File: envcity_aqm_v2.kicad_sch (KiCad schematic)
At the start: 136 parts, among them IC1 DS1307ZN+, IC2 DMMT5401-7F, IC3 DMMT5401-7F, IC4 DMMT5401-7-F, IC6 ESP32-S2-SOLO-N4R2, J1 USB_B_Micro, J10 Conn_01x06_Male, J11 Conn_01x06_Male, J12 Conn_01x06_Male, J13 Conn_01x06_Male, J14 Conn_01x08_Pin, J15 Conn_01x02_Male, J16 Conn_01x02_Male, J2 Screw_Terminal_01x02, J3 Screw_Terminal_01x02, J4 Micro_SD_Card, J5 Conn_01x03_Male, J6 Conn_01x04_Male, J7 Conn_01x06_Pin, J8 Conn_01x06_Male, J9 Conn_01x06_Male, Q1 DMG2301L / DMP2045U, Q2 DMG2301L / DMP2045U, Q3 DMG2301L, Q4 DMG2301L, Q5 DMG2301L / DMP2045U, Q6 DMG2301L, Q7 DMN10H220L, Q8 DMN10H220L, SW1 BOOT, SW1 RESET, U1 TP4056, U10 RFM95W-915S2, U11 ADS1115IDGS, U2 USBLC6-2SC6, U3 MT3608, U4 MT3608, U5 LM2596S-5, U6 AP2112K-3.3, U7 DHT11, U8 AP2112K-3.3, U9 74HC4067DB, Y2 AB26TRB

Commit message: Terminando o posicionamento dos components
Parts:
- added C35: 100nF, Capacitor_SMD:C_0603_1608Metric, symbol Device:C_Small
- C18, C19, C20, C21, C25, C26, C27: footprint Capacitor_SMD:C_0805_2012Metric -> Capacitor_SMD:C_0603_1608Metric
- J14: footprint Connector_PinHeader_2.54mm:PinHeader_1x08_P2.54mm_Vertical -> Connector_Molex:Molex_PicoBlade_53047-0810_1x08_P1.25mm_Vertical
- J7: footprint Connector_Molex:Molex_KK-254_AE-6410-06A_1x06_P2.54mm_Vertical -> Connector_PinHeader_2.54mm:PinHeader_1x06_P2.54mm_Vertical
- renumbered J8 to EQ1, J9 to EQ2, J10 to EQ3, J11 to EQ4
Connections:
- net +5V: now also C35.2
- net GND: now also C35.1
- net I12: now also J5.3 (Pin_3)
- net I7: no longer J5.3 (Pin_3)
- net RFM_CS: now also IC6.17 (IO9); no longer IC6.18 (IO10)
- net RFM_DIO0: now also IC6.25 (IO34); no longer IC6.23 (IO21)
- net RFM_DIO2: now also IC6.23 (IO21); no longer IC6.25 (IO34)
- net RFM_SCK: now also IC6.18 (IO10); no longer IC6.21 (IO13)
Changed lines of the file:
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@@
   (junction (at 213.36 238.76) (diameter 0) (color 0 0 0 0)
   )
+  (junction (at 90.17 285.75) (diameter 0) (color 0 0 0 0)
+  )
   (junction (at 361.95 261.62) (diameter 0) (color 0 0 0 0)
   )
@@
   (no_connect (at 66.04 337.82))
   (no_connect (at 486.41 270.51))
+  (no_connect (at 462.28 203.2))
   (no_connect (at 486.41 275.59))
   (no_connect (at 495.3 157.48))
@@
   (no_connect (at 334.01 196.85))
   (no_connect (at 462.28 180.34))
-  (no_connect (at 462.28 193.04))
   (no_connect (at 468.63 78.74))
   (no_connect (at 495.3 162.56))
@@
     (stroke (width 0) (type default))
   )
+  (wire (pts (xy 90.17 285.75) (xy 96.52 285.75))
+    (stroke (width 0) (type default))
+  )
   (wire (pts (xy 152.4 317.5) (xy 152.4 322.58))
     (stroke (width 0) (type default))
@@
     (stroke (width 0) (type default))
   )
-  (wire (pts (xy 457.2 195.58) (xy 462.28 195.58))
+  (wire (pts (xy 457.2 193.04) (xy 462.28 193.04))
     (stroke (width 0) (type default))
   )
@@
     (stroke (width 0) (type default))
   )
-  (wire (pts (xy 457.2 203.2) (xy 462.28 203.2))
+  (wire (pts (xy 457.2 195.58) (xy 462.28 195.58))
     (stroke (width 0) (type default))
   )
@@
     (stroke (width 0) (type default))
   )
+  (wire (pts (xy 101.6 285.75) (xy 102.87 285.75))
+    (stroke (width 0) (type default))
+  )
   (wire (pts (xy 501.65 195.58) (xy 501.65 198.12))
     (stroke (width 0) (type default))
@@
     (effects (font (size 1.27 1.27)) (justify left bottom))
   )
-  (label "RFM_DIO0" (at 457.2 208.28 180) (fields_autoplaced)
+  (label "RFM_DIO0" (at 457.2 213.36 180) (fields_autoplaced)
     (effects (font (size 1.27 1.27)) (justify right bottom))
   )
@@
     (effects (font (size 1.27 1.27)) (justify left bottom))
   )
-  (label "RFM_SCK" (at 457.2 203.2 180) (fields_autoplaced)
+  (label "RFM_SCK" (at 457.2 195.58 180) (fields_autoplaced)
     (effects (font (size 1.27 1.27)) (justify right bottom))
   )
@@
     (effects (font (size 1.27 1.27)) (justify left bottom))
   )
-  (label "RFM_DIO2" (at 457.2 213.36 180) (fields_autoplaced)
+  (label "RFM_DIO2" (at 457.2 208.28 180) (fields_autoplaced)
     (effects (font (size 1.27 1.27)) (justify right bottom))
   )
@@
     (effects (font (size 1.27 1.27)) (justify left bottom))
   )
-  (label "I7" (at 294.64 234.95 0) (fields_autoplaced)
+  (label "I12" (at 294.64 234.95 0) (fields_autoplaced)
     (effects (font (size 1.27 1.27)) (justify left bottom))
   )
@@
     (effects (font (size 1.27 1.27)) (justify right bottom))
   )
-  (label "RFM_CS" (at 457.2 195.58 180) (fields_autoplaced)
+  (label "RFM_CS" (at 457.2 193.04 180) (fields_autoplaced)
     (effects (font (size 1.27 1.27)) (justify right bottom))
   )
@@
   (symbol (lib_id "envcity_aqm_v2-rescue:Conn_01x06_Male-Connector") (at 325.12 227.33 0) (unit 1)
     (in_bom yes) (on_board yes) (dnp no)
-    (property "Reference" "J8" (at 327.66 215.9 0)
+    (property "Reference" "EQ1" (at 327.66 215.9 0)
       (effects (font (size 1.27 1.27)))
     )
@@
       (project "envcity_aqm_v2"
         (path "/332e6a95-8453-45a7-bff6-50b465637d27"
-          (reference "J8") (unit 1)
+          (reference "EQ1") (unit 1)
         )
       )
@@
   (symbol (lib_id "envcity_aqm_v2-rescue:Conn_01x06_Male-Connector") (at 350.52 227.33 0) (unit 1)
     (in_bom yes) (on_board yes) (dnp no)
-    (property "Reference" "J9" (at 353.06 215.9 0)
+    (property "Reference" "EQ2" (at 353.06 215.9 0)
       (effects (font (size 1.27 1.27)))
     )
@@
       (project "envcity_aqm_v2"
         (path "/332e6a95-8453-45a7-bff6-50b465637d27"
-          (reference "J9") (unit 1)
+          (reference "EQ2") (unit 1)
         )
       )
@@
   (symbol (lib_id "envcity_aqm_v2-rescue:Conn_01x06_Male-Connector") (at 325.12 252.73 0) (unit 1)
     (in_bom yes) (on_board yes) (dnp no)
-    (property "Reference" "J10" (at 327.66 241.3 0)
+    (property "Reference" "EQ3" (at 327.66 241.3 0)
       (effects (font (size 1.27 1.27)))
     )
@@
       (project "envcity_aqm_v2"
         (path "/332e6a95-8453-45a7-bff6-50b465637d27"
-          (reference "J10") (unit 1)
+          (reference "EQ3") (unit 1)
         )
       )
@@
   (symbol (lib_id "envcity_aqm_v2-rescue:Conn_01x06_Male-Connector") (at 350.52 254 0) (unit 1)
     (in_bom yes) (on_board yes) (dnp no)
-    (property "Reference" "J11" (at 353.06 241.3 0)
+    (property "Reference" "EQ4" (at 353.06 241.3 0)
       (effects (font (size 1.27 1.27)))
     )
@@
       (project "envcity_aqm_v2"
         (path "/332e6a95-8453-45a7-bff6-50b465637d27"
-          (reference "J11") (unit 1)
+          (reference "EQ4") (unit 1)
         )
       )
@@
       (effects (font (size 1.27 1.27)) (justify left))
     )
-    (property "Footprint" "Capacitor_SMD:C_0805_2012Metric" (at 367.03 227.33 0)
+    (property "Footprint" "Capacitor_SMD:C_0603_1608Metric" (at 367.03 227.33 0)
       (effects (font (size 1.27 1.27)) hide)
     )
@@
       (effects (font (size 1.27 1.27)) (justify left))
     )
-    (property "Footprint" "Capacitor_SMD:C_0805_2012Metric" (at 341.63 227.33 0)
+    (property "Footprint" "Capacitor_SMD:C_0603_1608Metric" (at 341.63 227.33 0)
       (effects (font (size 1.27 1.27)) hide)
     )
@@
       (effects (font (size 1.27 1.27)) (justify left))
     )
-    (property "Footprint" "Capacitor_SMD:C_0805_2012Metric" (at 340.36 252.73 0)
+    (property "Footprint" "Capacitor_SMD:C_0603_1608Metric" (at 340.36 252.73 0)
       (effects (font (size 1.27 1.27)) hide)
     )
@@
       (effects (font (size 1.27 1.27)) (justify left))
     )
-    (property "Footprint" "Capacitor_SMD:C_0805_2012Metric" (at 365.76 252.73 0)
+    (property "Footprint" "Capacitor_SMD:C_0603_1608Metric" (at 365.76 252.73 0)
       (effects (font (size 1.27 1.27)) hide)
     )
@@
     )
   )
+  (symbol (lib_id "Device:C_Small") (at 99.06 285.75 270) (mirror x) (unit 1)
+    (in_bom yes) (on_board yes) (dnp no)
+    (property "Reference" "C35" (at 100.2284 283.4132 0)
+      (effects (font (size 1.27 1.27)) (justify left))
+    )
+    (property "Value" "100nF" (at 97.917 283.4132 0)
+      (effects (font (size 1.27 1.27)) (justify left))
+    )
+    (property "Footprint" "Capacitor_SMD:C_0603_1608Metric" (at 99.06 285.75 0)
+      (effects (font (size 1.27 1.27)) hide)
+    )
+    (property "Datasheet" "~" (at 99.06 285.75 0)
+      (effects (font (size 1.27 1.27)) hide)
+    )
+    (pin "1")
+    (pin "2")
+    (instances
+      (project "envcity_aqm_v2"
+        (path "/332e6a95-8453-45a7-bff6-50b465637d27"
+          (reference "C35") (unit 1)
+        )
+      )
+    )
+  )
   (symbol (lib_id "DMMT5401-7-F:DMMT5401-7-F") (at 247.65 34.29 0) (mirror x) (unit 2)
     (in_bom yes) (on_board yes) (dnp no)
@@
       (effects (font (size 1.27 1.27)) (justify left))
     )
-    (property "Footprint" "Capacitor_SMD:C_0805_2012Metric" (at 365.76 278.13 0)
+    (property "Footprint" "Capacitor_SMD:C_0603_1608Metric" (at 365.76 278.13 0)
       (effects (font (size 1.27 1.27)) hide)
     )
@@
       (effects (font (size 1.27 1.27)))
     )
-    (property "Footprint" "Connector_Molex:Molex_KK-254_AE-6410-06A_1x06_P2.54mm_Vertical" (at 285.75 313.69 0)
+    (property "Footprint" "Connector_PinHeader_2.54mm:PinHeader_1x06_P2.54mm_Vertical" (at 285.75 313.69 0)
       (effects (font (size 1.27 1.27)) hide)
     )
@@
       (effects (font (size 1.27 1.27)) (justify left))
     )
-    (property "Footprint" "Capacitor_SMD:C_0805_2012Metric" (at 340.36 278.13 0)
+    (property "Footprint" "Capacitor_SMD:C_0603_1608Metric" (at 340.36 278.13 0)
       (effects (font (size 1.27 1.27)) hide)
     )
@@
       (effects (font (size 1.27 1.27)))
     )
-    (property "Footprint" "Connector_PinHeader_2.54mm:PinHeader_1x08_P2.54mm_Vertical" (at 328.93 186.69 0)
+    (property "Footprint" "Connector_Molex:Molex_PicoBlade_53047-0810_1x08_P1.25mm_Vertical" (at 328.93 186.69 0)
       (effects (font (size 1.27 1.27)) hide)
     )
@@
     )
   )
+  (symbol (lib_id "power:GND") (at 102.87 285.75 90) (unit 1)
+    (in_bom yes) (on_board yes) (dnp no) (fields_autoplaced)
+    (property "Reference" "#PWR0108" (at 109.22 285.75 0)
+      (effects (font (size 1.27 1.27)) hide)
+    )
+    (property "Value" "GND" (at 106.045 286.0668 90)
+      (effects (font (size 1.27 1.27)) (justify right))
+    )
+    (property "Footprint" "" (at 102.87 285.75 0)
+      (effects (font (size 1.27 1.27)) hide)
+    )
+    (property "Datasheet" "" (at 102.87 285.75 0)
+      (effects (font (size 1.27 1.27)) hide)
+    )
+    (pin "1")
+    (instances
+      (project "envcity_aqm_v2"
+        (path "/332e6a95-8453-45a7-bff6-50b465637d27"
+          (reference "#PWR0108") (unit 1)
+        )
+      )
+    )
+  )
   (symbol (lib_id "power:+3V3") (at 354.33 177.8 0) (unit 1)
     (in_bom yes) (on_board yes) (dnp no) (fields_autoplaced)
@@
       (effects (font (size 1.27 1.27)) (justify left))
     )
-    (property "Footprint" "Capacitor_SMD:C_0805_2012Metric" (at 342.9 179.07 0)
+    (property "Footprint" "Capacitor_SMD:C_0603_1608Metric" (at 342.9 179.07 0)
       (effects (font (size 1.27 1.27)) hide)
     )

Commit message: mudando posicoes
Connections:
- net DHT_PIN: now also IC6.28 (IO35); no longer IC6.35 (IO42)
- no-connect marks 23 -> 22
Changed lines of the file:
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@@
   (no_connect (at 462.28 203.2))
   (no_connect (at 486.41 275.59))
-  (no_connect (at 495.3 157.48))
   (no_connect (at 495.3 152.4))
   (no_connect (at 334.01 196.85))
@@
     (stroke (width 0) (type default))
   )
-  (wire (pts (xy 495.3 175.26) (xy 501.65 175.26))
-    (stroke (width 0) (type default))
-  )
   (wire (pts (xy 340.36 247.65) (xy 337.82 247.65))
     (stroke (width 0) (type default))
@@
   )
   (wire (pts (xy 290.83 194.31) (xy 290.83 196.85))
+    (stroke (width 0) (type default))
+  )
+  (wire (pts (xy 495.3 157.48) (xy 499.11 157.48))
     (stroke (width 0) (type default))
   )
@@
     (effects (font (size 0.9906 0.9906)) (justify left bottom))
   )
-  (label "DHT_PIN" (at 501.65 175.26 0) (fields_autoplaced)
-    (effects (font (size 1.27 1.27)) (justify left bottom))
-  )
+  (label "DHT_PIN" (at 499.11 157.48 0) (fields_autoplaced)
+    (effects (font (size 1.27 1.27)) (justify left bottom))
+  )

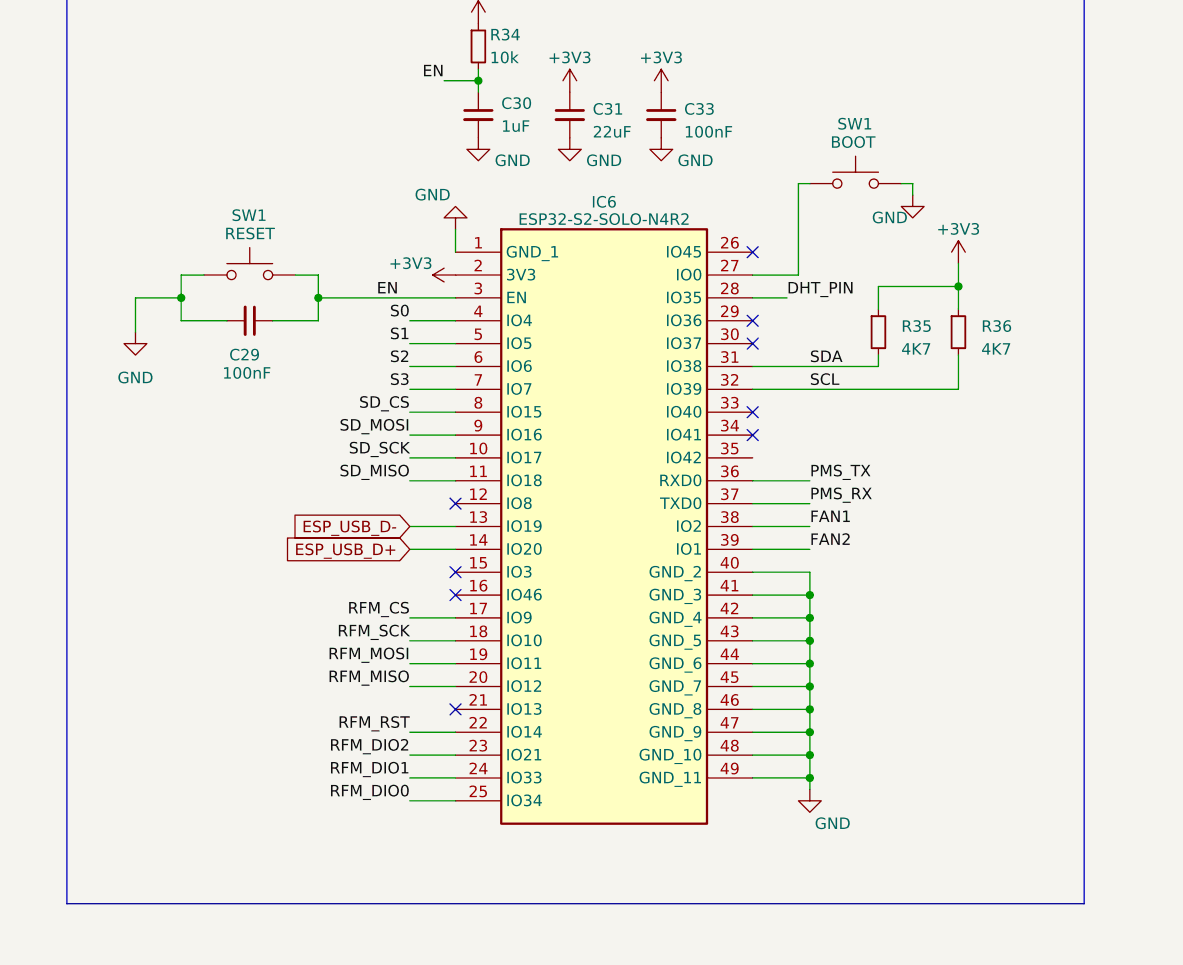
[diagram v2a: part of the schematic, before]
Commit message: Alteracoes no roteamento
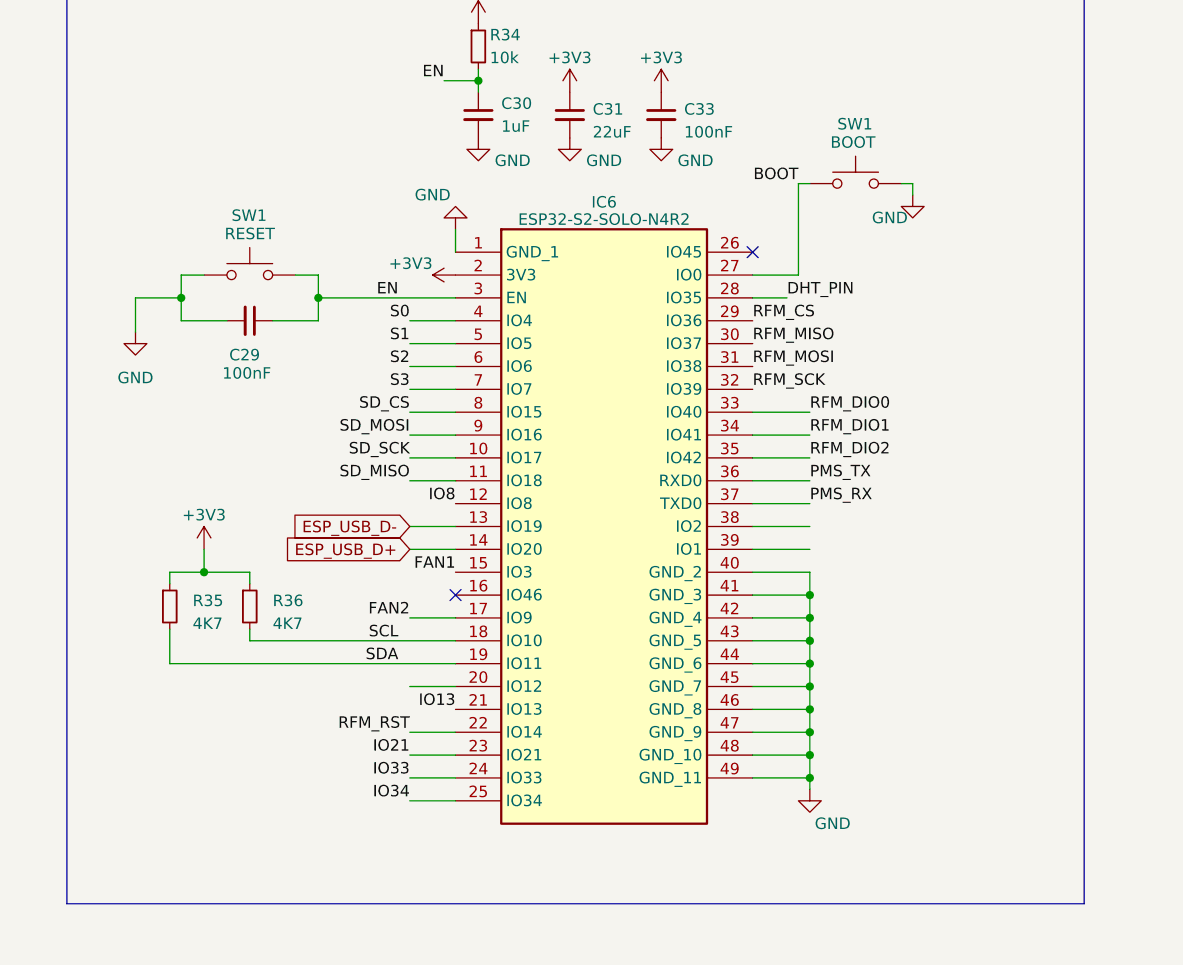
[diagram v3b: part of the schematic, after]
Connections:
- net FAN1: now also IC6.15 (IO3); no longer IC6.38 (IO2)
- net FAN2: now also IC6.17 (IO9); no longer IC6.39 (IO1)
- net RFM_CS: now also IC6.29 (IO36); no longer IC6.17 (IO9)
- net RFM_DIO0: now also IC6.33 (IO40); no longer IC6.25 (IO34)
- net RFM_DIO1: now also IC6.34 (IO41); no longer IC6.24 (IO33)
- net RFM_DIO2: now also IC6.35 (IO42); no longer IC6.23 (IO21)
- net RFM_MISO: now also IC6.30 (IO37); no longer IC6.20 (IO12)
- net RFM_MOSI: now also IC6.31 (IO38); no longer IC6.19 (IO11)
- net RFM_SCK: now also IC6.32 (IO39); no longer IC6.18 (IO10)
- net SCL: now also IC6.18 (IO10); no longer IC6.32 (IO39)
- net SDA: now also IC6.19 (IO11); no longer IC6.31 (IO38)
- net IO8: now reaches IC6.12 (IO8)
- net IO13: now reaches IC6.21 (IO13)
- net BOOT: now reaches IC6.27 (IO0), SW1.1
- new net IO21: IC6.23 (IO21)
- new net IO33: IC6.24 (IO33)
- new net IO34: IC6.25 (IO34)
- no-connect marks 22 -> 15
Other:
- moved on the sheet: R35, R36

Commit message: add 3d model pms. add mais trilhas
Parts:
- removed D6: 5V, Diode_SMD:D_SOD-323, symbol envcity_aqm_v2-rescue:D_Zener_ALT-Device
- removed R28, R29: 10k, Resistor_SMD:R_0805_2012Metric, symbol Device:R_Small
- removed R5: 1K, Resistor_SMD:R_0805_2012Metric, symbol Device:R
- C17: footprint Capacitor_SMD:C_0805_2012Metric -> Capacitor_SMD:C_0603_1608Metric
- R1, R10, R15, R19, R20, R24, R27, R8: footprint Resistor_SMD:R_0805_2012Metric -> Resistor_SMD:R_0603_1608Metric
- R30, R31, R32, R33: footprint Resistor_SMD:R_0603_1608Metric -> Resistor_SMD:R_0402_1005Metric_Pad0.72x0.64mm_HandSolder
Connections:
- net IO21 is gone; now on net DHT_PIN: IC6.23 (IO21)
- net IO34 is gone; now on net PMS_TX: IC6.25 (IO34)
- net DHT_PIN: no longer IC6.28 (IO35)
- net GND: now also Q2.1 (G)
- net PMS_RX: now also IC6.28 (IO35); no longer IC6.37 (TXD0)
- net PMS_TX: no longer IC6.36 (RXD0)
- net SCL: now also IC6.19 (IO11), R35.2; no longer IC6.18 (IO10), R36.2
- net SDA: now also IC6.18 (IO10), R36.2; no longer IC6.19 (IO11), R35.2
- net IO12: now reaches IC6.20 (IO12)
- net IO2: now reaches IC6.38 (IO2)
- net IO1: now reaches IC6.39 (IO1)
- no-connect marks 15 -> 19

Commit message: add trilhas
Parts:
- R13, R14, R16, R17, R18, R2, R23, R3: footprint Resistor_SMD:R_0805_2012Metric -> Resistor_SMD:R_0603_1608Metric
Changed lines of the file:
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@@
       (effects (font (size 1.27 1.27)) (justify left))
     )
-    (property "Footprint" "Resistor_SMD:R_0805_2012Metric" (at 243.332 308.61 90)
+    (property "Footprint" "Resistor_SMD:R_0603_1608Metric" (at 243.332 308.61 90)
       (effects (font (size 1.27 1.27)) hide)
     )
@@
       (effects (font (size 1.27 1.27)) (justify left))
     )
-    (property "Footprint" "Resistor_SMD:R_0805_2012Metric" (at 242.062 184.15 90)
+    (property "Footprint" "Resistor_SMD:R_0603_1608Metric" (at 242.062 184.15 90)
       (effects (font (size 1.27 1.27)) hide)
     )
@@
       (effects (font (size 1.27 1.27)) (justify left))
     )
-    (property "Footprint" "Resistor_SMD:R_0805_2012Metric" (at 103.632 196.85 90)
+    (property "Footprint" "Resistor_SMD:R_0603_1608Metric" (at 103.632 196.85 90)
       (effects (font (size 1.27 1.27)) hide)
     )
@@
       (effects (font (size 1.27 1.27)) (justify left))
     )
-    (property "Footprint" "Resistor_SMD:R_0805_2012Metric" (at 94.742 196.85 90)
+    (property "Footprint" "Resistor_SMD:R_0603_1608Metric" (at 94.742 196.85 90)
       (effects (font (size 1.27 1.27)) hide)
     )
@@
       (effects (font (size 1.27 1.27)) (justify left))
     )
-    (property "Footprint" "Resistor_SMD:R_0805_2012Metric" (at 209.55 255.27 0)
+    (property "Footprint" "Resistor_SMD:R_0603_1608Metric" (at 209.55 255.27 0)
       (effects (font (size 1.27 1.27)) hide)
     )
@@
       (effects (font (size 1.27 1.27)) (justify left))
     )
-    (property "Footprint" "Resistor_SMD:R_0805_2012Metric" (at 209.55 245.11 0)
+    (property "Footprint" "Resistor_SMD:R_0603_1608Metric" (at 209.55 245.11 0)
       (effects (font (size 1.27 1.27)) hide)
     )
@@
       (effects (font (size 1.27 1.27)) (justify left))
     )
-    (property "Footprint" "Resistor_SMD:R_0805_2012Metric" (at 245.872 240.03 90)
+    (property "Footprint" "Resistor_SMD:R_0603_1608Metric" (at 245.872 240.03 90)
       (effects (font (size 1.27 1.27)) hide)
     )
@@
       (effects (font (size 1.27 1.27)) (justify left))
     )
-    (property "Footprint" "Resistor_SMD:R_0805_2012Metric" (at 316.484 373.634 90)
+    (property "Footprint" "Resistor_SMD:R_0603_1608Metric" (at 316.484 373.634 90)
       (effects (font (size 1.27 1.27)) hide)
     )

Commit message: Trocando o modelo do cartaoSD
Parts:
- added J8: 503398-1892, Molex 503398-1892:503398-1892, symbol 503398-1892:503398-1892
- added R28, R29, R4, R5: 10k, Resistor_SMD:R_0402_1005Metric, symbol Device:R_Small
- H1: footprint MountingHole:MountingHole_2.5mm -> MountingHole:MountingHole_2.2mm_M2
- J4: value Micro_SD_Card -> MicroSD_Card MOLEX 5033981892; LCSC Part# (none) -> C428492
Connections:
- net IO1 is gone; now on net S0: IC6.39 (IO1)
- net IO2 is gone; now on net S1: IC6.38 (IO2)
- net +3V3: now also J8.4 (VDD), R28.1, R29.1, R4.1, R5.1; no longer J4.4 (VDD)
- net GND: now also J8.6 (VSS); no longer J4.6 (VSS), J4.9 (SHIELD)
- net S0: no longer IC6.4 (IO4)
- net S1: no longer IC6.5 (IO5)
- net S2: now also IC6.10 (IO17); no longer IC6.6 (IO6)
- net S3: now also IC6.11 (IO18); no longer IC6.7 (IO7)
- net SD_CS: now also IC6.5 (IO5), J8.2 (CD/DAT3), R5.2; no longer IC6.8 (IO15), J4.2 (DAT3/CD)
- net SD_MISO: now also IC6.8 (IO15), J8.7 (DAT0), R29.2; no longer IC6.11 (IO18), J4.7 (DAT0)
- net SD_MOSI: now also IC6.6 (IO6), J8.3 (CMD); no longer IC6.9 (IO16), J4.3 (CMD)
- net SD_SCK: now also IC6.7 (IO7), J8.5 (CLK); no longer IC6.10 (IO17), J4.5 (CLK)
- new net DAT1: J8.8 (DAT1), R28.2
- new net DAT2: J8.1 (DAT2), R4.2
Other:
- moved on the sheet: C1, C2, J4
